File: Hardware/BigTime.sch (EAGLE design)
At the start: 18 parts, among them J1 AVR_SPI_PRG_6TESTPOINTS-SM, U2 ATMEGA328P_TQFP, Y1 32.768kHz

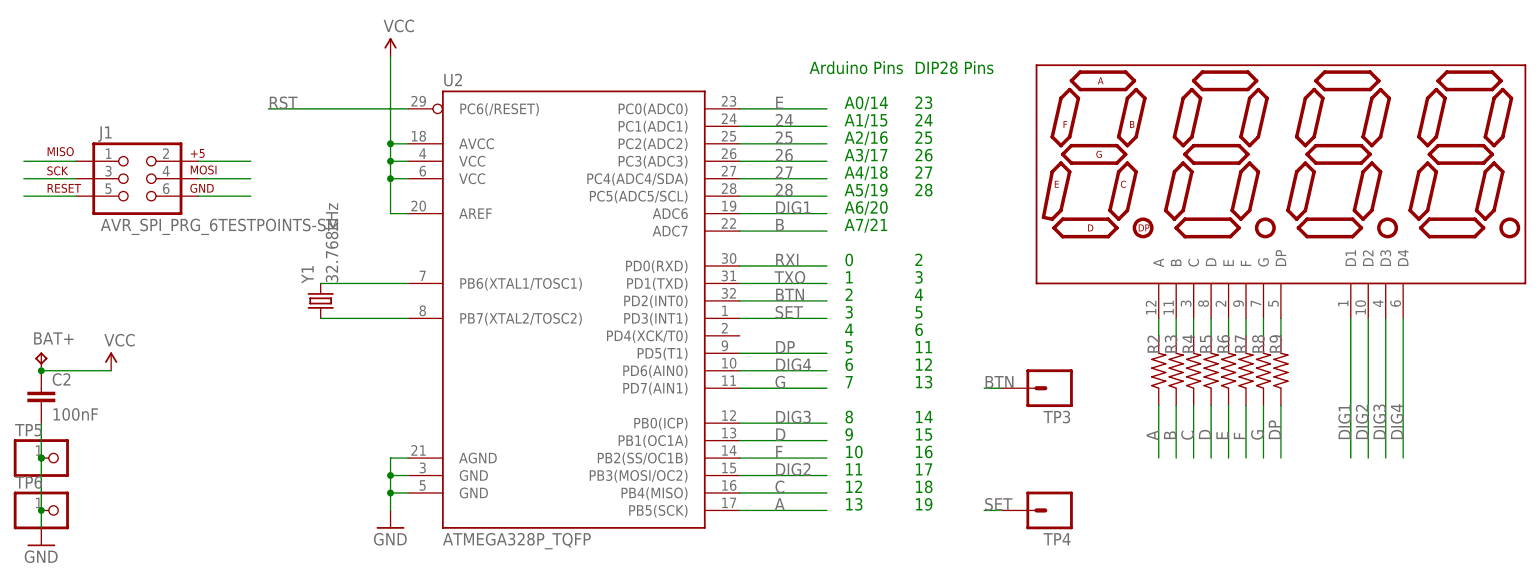
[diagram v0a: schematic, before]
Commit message: Reroute pins
Can't use A6 and A7 as digital outs
Use bigger traces and more spacing
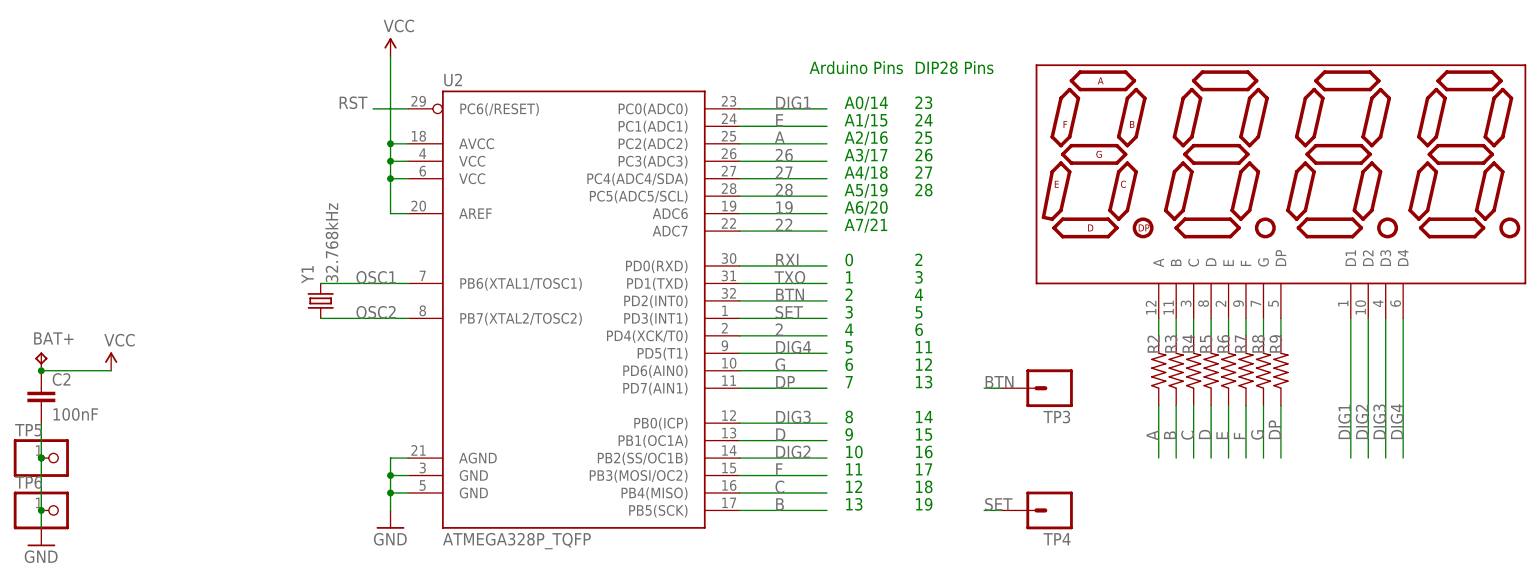
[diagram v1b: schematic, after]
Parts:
- removed J1: AVR_SPI_PRG_6TESTPOINTS-SM, Connectors:AVR_SPI_PRG_6TESTPOINTS-SM
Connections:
- net N$1 renamed OSC2
- net N$10 renamed G'
- net N$11 renamed DP'
- net N$2 renamed OSC1
- net N$4 renamed A'
- net N$5 renamed B'
- net N$6 renamed C'
- net N$7 renamed D'
- net N$8 renamed E'
- net N$9 renamed F'
- removed net 24: U2.PC1(ADC1)
- removed net 25: U2.PC2(ADC2)
- new net 19: U2.ADC6
- new net 2: U2.PD4(XCK/T0)
- new net 22: U2.ADC7
- net A: now also U2.PC2(ADC2); no longer J1.3, U2.PB5(SCK)
- net B: now also U2.PB5(SCK); no longer U2.ADC7
- net C: no longer J1.1
- net DIG1: now also U2.PC0(ADC0); no longer U2.ADC6
- net DIG2: now also U2.PB2(SS/OC1B); no longer J1.4, U2.PB3(MOSI/OC2)
- net DIG4: now also U2.PD5(T1); no longer U2.PD6(AIN0)
- net DP: now also U2.PD7(AIN1); no longer U2.PD5(T1)
- net E: now also U2.PC1(ADC1); no longer U2.PC0(ADC0)
- net F: now also U2.PB3(MOSI/OC2); no longer U2.PB2(SS/OC1B)
- net G: now also U2.PD6(AIN0); no longer U2.PD7(AIN1)
- net GND: no longer J1.6
- net RST: no longer J1.5
- net VCC: no longer J1.2

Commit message: redesign again
smaller battery, move ic to back, crystal to front, remap pins
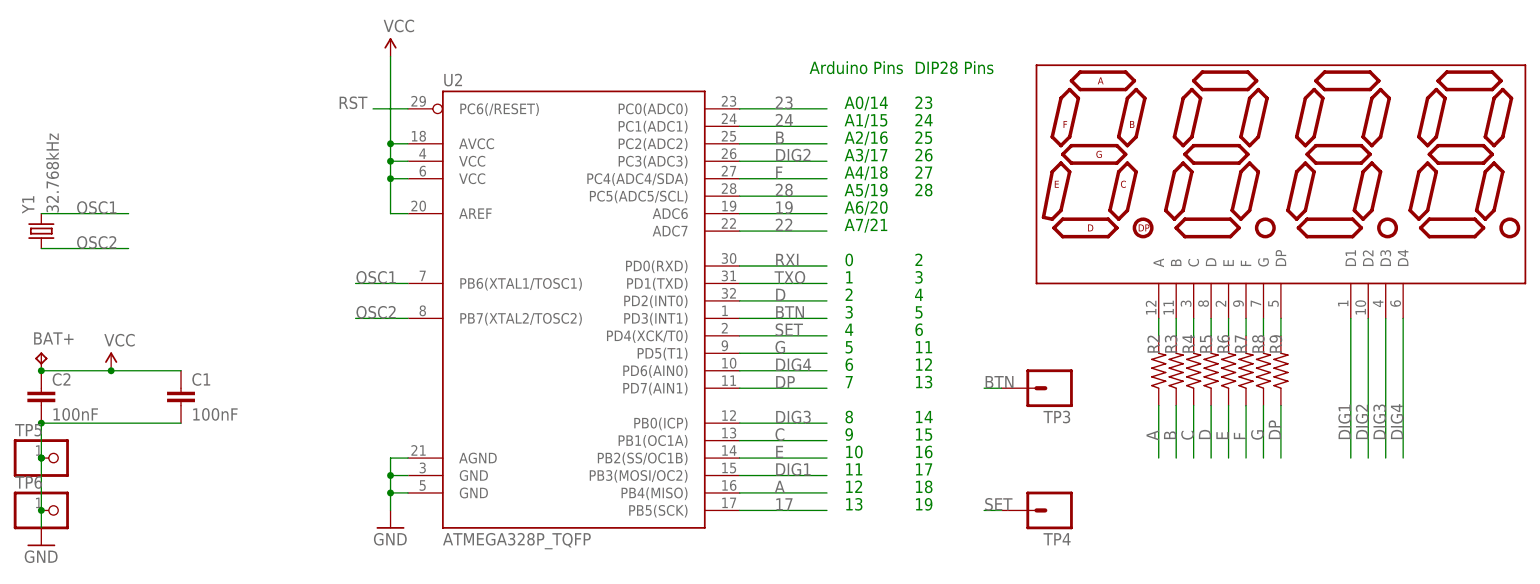
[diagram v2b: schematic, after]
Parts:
- added C1: 100nF, resistor:C-EUC0805
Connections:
- removed net 2: U2.PD4(XCK/T0)
- removed net 26: U2.PC3(ADC3)
- removed net 27: U2.PC4(ADC4/SDA)
- new net 17: U2.PB5(SCK)
- new net 23: U2.PC0(ADC0)
- new net 24: U2.PC1(ADC1)
- net A: now also U2.PB4(MISO); no longer U2.PC2(ADC2)
- net B: now also U2.PC2(ADC2); no longer U2.PB5(SCK)
- net BTN: now also U2.PD3(INT1); no longer U2.PD2(INT0)
- net C: now also U2.PB1(OC1A); no longer U2.PB4(MISO)
- net D: now also U2.PD2(INT0); no longer U2.PB1(OC1A)
- net DIG1: now also U2.PB3(MOSI/OC2); no longer U2.PC0(ADC0)
- net DIG2: now also U2.PC3(ADC3); no longer U2.PB2(SS/OC1B)
- net DIG4: now also U2.PD6(AIN0); no longer U2.PD5(T1)
- net E: now also U2.PB2(SS/OC1B); no longer U2.PC1(ADC1)
- net F: now also U2.PC4(ADC4/SDA); no longer U2.PB3(MOSI/OC2)
- net G: now also U2.PD5(T1); no longer U2.PD6(AIN0)
- net GND: now also C1.2
- net SET: now also U2.PD4(XCK/T0); no longer U2.PD3(INT1)
- net VCC: now also C1.1
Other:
- moved on the sheet: Y1
